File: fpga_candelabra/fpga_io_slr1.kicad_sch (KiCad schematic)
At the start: 1 part, among them U1 XCVU13P-B2104

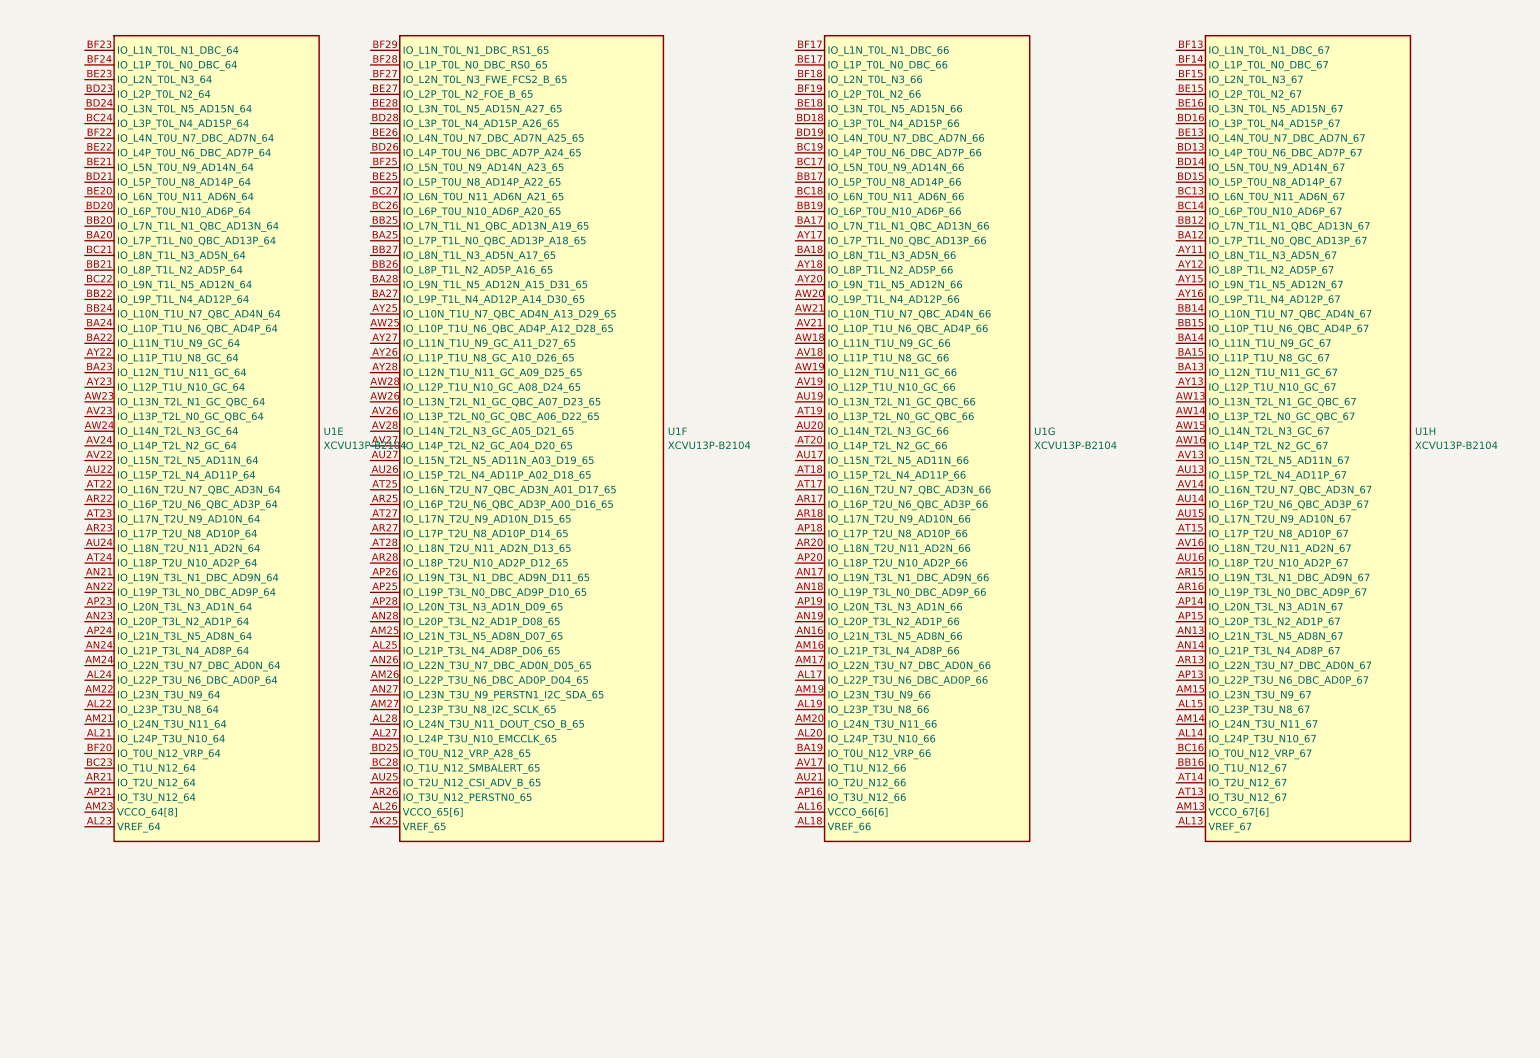
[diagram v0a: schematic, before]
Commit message: candelabra: add i-pex extension ports, remove FMC1
* update bank/mgt allocation
* add basic pcb floorplanning

Signed-off-by: Yichuan Gao <gaoyichuan000@gmail.com>
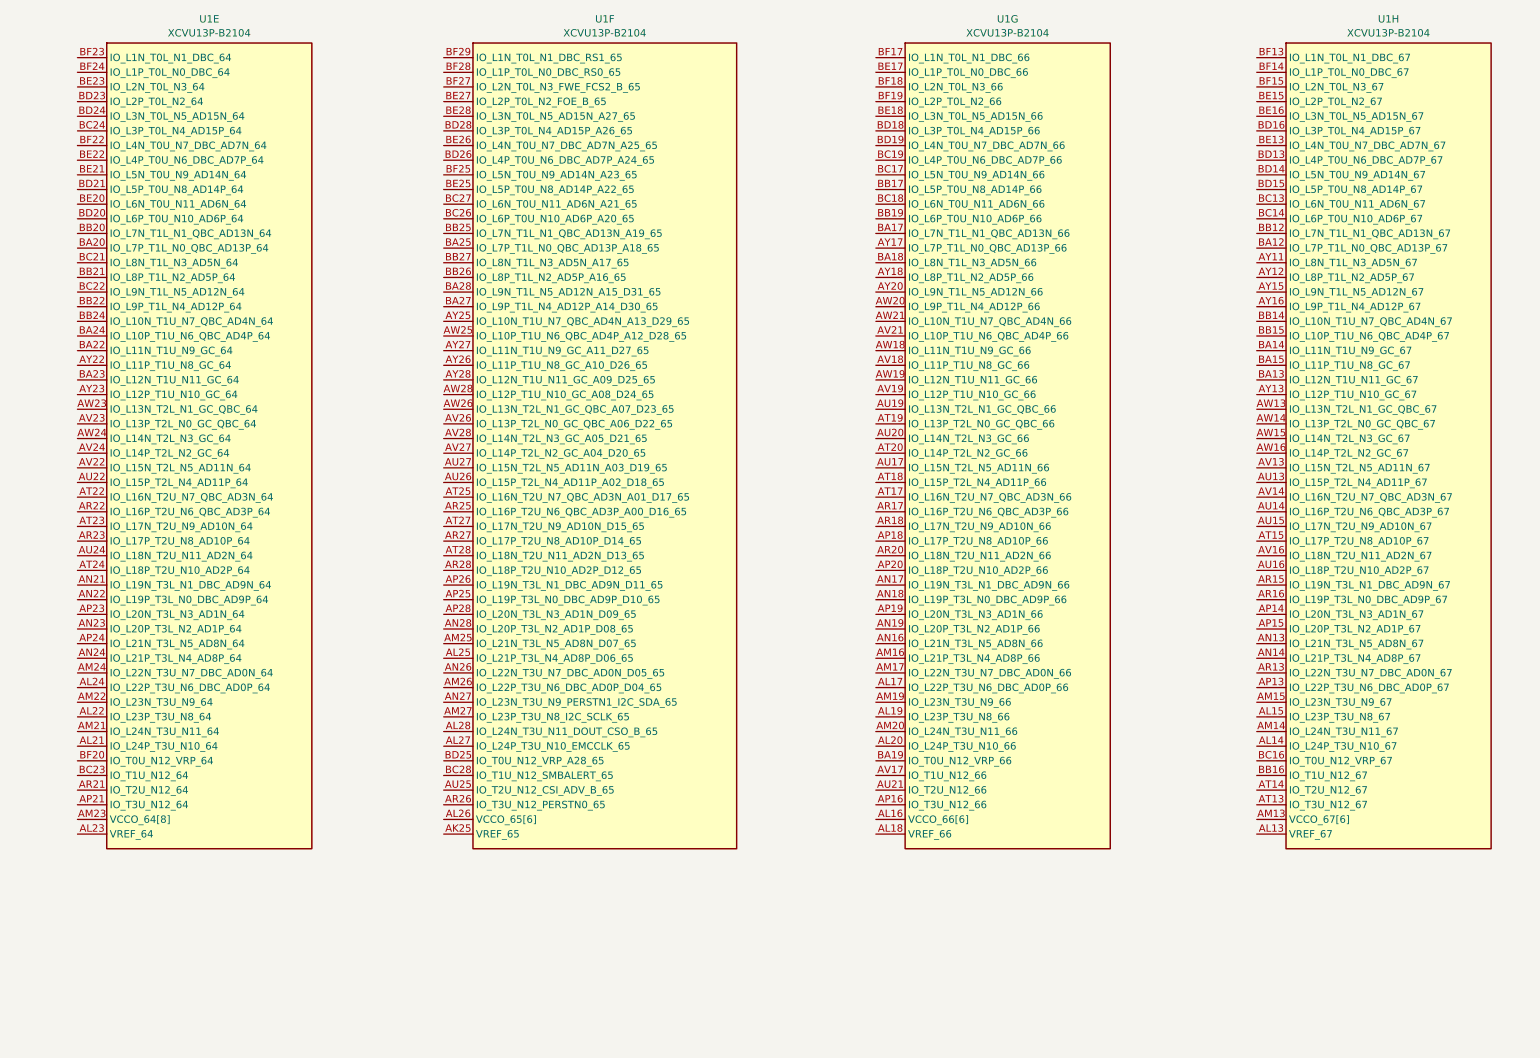
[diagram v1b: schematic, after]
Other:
- moved on the sheet: U1E, U1F, U1G, U1H
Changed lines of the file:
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@@
 	(symbol
 		(lib_id "CHIPSAlliance_FPGA_Xilinx_Virtex_UltraScale_Plus:XCVU13P-B2104")
-		(at 218.44 24.13 0)
+		(at 232.41 25.4 0)
 		(unit 8)
 		(exclude_from_sim no)
@@
 		(fields_autoplaced yes)
 		(property "Reference" "U1"
-			(at 259.842 90.2278 0)
+			(at 255.27 18.7155 0)
 			(effects
 				(font
 					(size 1.27 1.27)
 				)
-				(justify left)
 			)
 		)
 		(property "Value" "XCVU13P-B2104"
-			(at 259.842 92.6521 0)
+			(at 255.27 21.1398 0)
 			(effects
 				(font
 					(size 1.27 1.27)
 				)
-				(justify left)
 			)
 		)
 		(property "Footprint" "CHIPSAlliance_Package_BGA:Xilinx_FHGB2104_VU13P_PkgLength"
-			(at 217.17 22.86 0)
+			(at 231.14 24.13 0)
 			(effects
 				(font
@@
 		)
 		(property "Datasheet" ""
-			(at 217.17 60.96 0)
+			(at 231.14 62.23 0)
 			(effects
 				(font
@@
 		)
 		(property "Description" "Virtex UltraScale+ 13P XCVU13P-B2104"
-			(at 218.44 24.13 0)
+			(at 232.41 25.4 0)
 			(effects
 				(font
@@
 	(symbol
 		(lib_id "CHIPSAlliance_FPGA_Xilinx_Virtex_UltraScale_Plus:XCVU13P-B2104")
-		(at 29.21 24.13 0)
+		(at 27.94 25.4 0)
 		(unit 5)
 		(exclude_from_sim no)
@@
 		(fields_autoplaced yes)
 		(property "Reference" "U1"
-			(at 70.612 90.2278 0)
+			(at 50.8 18.7155 0)
 			(effects
 				(font
 					(size 1.27 1.27)
 				)
-				(justify left)
 			)
 		)
 		(property "Value" "XCVU13P-B2104"
-			(at 70.612 92.6521 0)
+			(at 50.8 21.1398 0)
 			(effects
 				(font
 					(size 1.27 1.27)
 				)
-				(justify left)
 			)
 		)
 		(property "Footprint" "CHIPSAlliance_Package_BGA:Xilinx_FHGB2104_VU13P_PkgLength"
-			(at 27.94 22.86 0)
+			(at 26.67 24.13 0)
 			(effects
 				(font
@@
 		)
 		(property "Datasheet" ""
-			(at 27.94 60.96 0)
+			(at 26.67 62.23 0)
 			(effects
 				(font
@@
 		)
 		(property "Description" "Virtex UltraScale+ 13P XCVU13P-B2104"
-			(at 29.21 24.13 0)
+			(at 27.94 25.4 0)
 			(effects
 				(font
@@
 	(symbol
 		(lib_id "CHIPSAlliance_FPGA_Xilinx_Virtex_UltraScale_Plus:XCVU13P-B2104")
-		(at 152.4 24.13 0)
+		(at 166.37 25.4 0)
 		(unit 7)
 		(exclude_from_sim no)
@@
 		(fields_autoplaced yes)
 		(property "Reference" "U1"
-			(at 193.802 90.2278 0)
+			(at 189.23 18.7155 0)
 			(effects
 				(font
 					(size 1.27 1.27)
 				)
-				(justify left)
 			)
 		)
 		(property "Value" "XCVU13P-B2104"
-			(at 193.802 92.6521 0)
+			(at 189.23 21.1398 0)
 			(effects
 				(font
 					(size 1.27 1.27)
 				)
-				(justify left)
 			)
 		)
 		(property "Footprint" "CHIPSAlliance_Package_BGA:Xilinx_FHGB2104_VU13P_PkgLength"
-			(at 151.13 22.86 0)
+			(at 165.1 24.13 0)
 			(effects
 				(font
@@
 		)
 		(property "Datasheet" ""
-			(at 151.13 60.96 0)
+			(at 165.1 62.23 0)
 			(effects
 				(font
@@
 		)
 		(property "Description" "Virtex UltraScale+ 13P XCVU13P-B2104"
-			(at 152.4 24.13 0)
+			(at 166.37 25.4 0)
 			(effects
 				(font
@@
 	(symbol
 		(lib_id "CHIPSAlliance_FPGA_Xilinx_Virtex_UltraScale_Plus:XCVU13P-B2104")
-		(at 78.74 24.13 0)
+		(at 91.44 25.4 0)
 		(unit 6)
 		(exclude_from_sim no)
@@
 		(fields_autoplaced yes)
 		(property "Reference" "U1"
-			(at 130.302 90.2278 0)
+			(at 119.38 18.7155 0)
 			(effects
 				(font
 					(size 1.27 1.27)
 				)
-				(justify left)
 			)
 		)
 		(property "Value" "XCVU13P-B2104"
-			(at 130.302 92.6521 0)
+			(at 119.38 21.1398 0)
 			(effects
 				(font
 					(size 1.27 1.27)
 				)
-				(justify left)
 			)
 		)
 		(property "Footprint" "CHIPSAlliance_Package_BGA:Xilinx_FHGB2104_VU13P_PkgLength"
-			(at 77.47 22.86 0)
+			(at 90.17 24.13 0)
 			(effects
 				(font
@@
 		)
 		(property "Datasheet" ""
-			(at 77.47 60.96 0)
+			(at 90.17 62.23 0)
 			(effects
 				(font
@@
 		)
 		(property "Description" "Virtex UltraScale+ 13P XCVU13P-B2104"
-			(at 78.74 24.13 0)
+			(at 91.44 25.4 0)
 			(effects
 				(font

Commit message: fpga_candelabra: major revision
* Finish DDR4 & QSFP+ & PCIe layout
* Change FMC to LPC
* Add mikroBUS extension
* 12V input & PDN updates
* FPGA config updates

Signed-off-by: Yichuan Gao <gaoyichuan000@gmail.com>
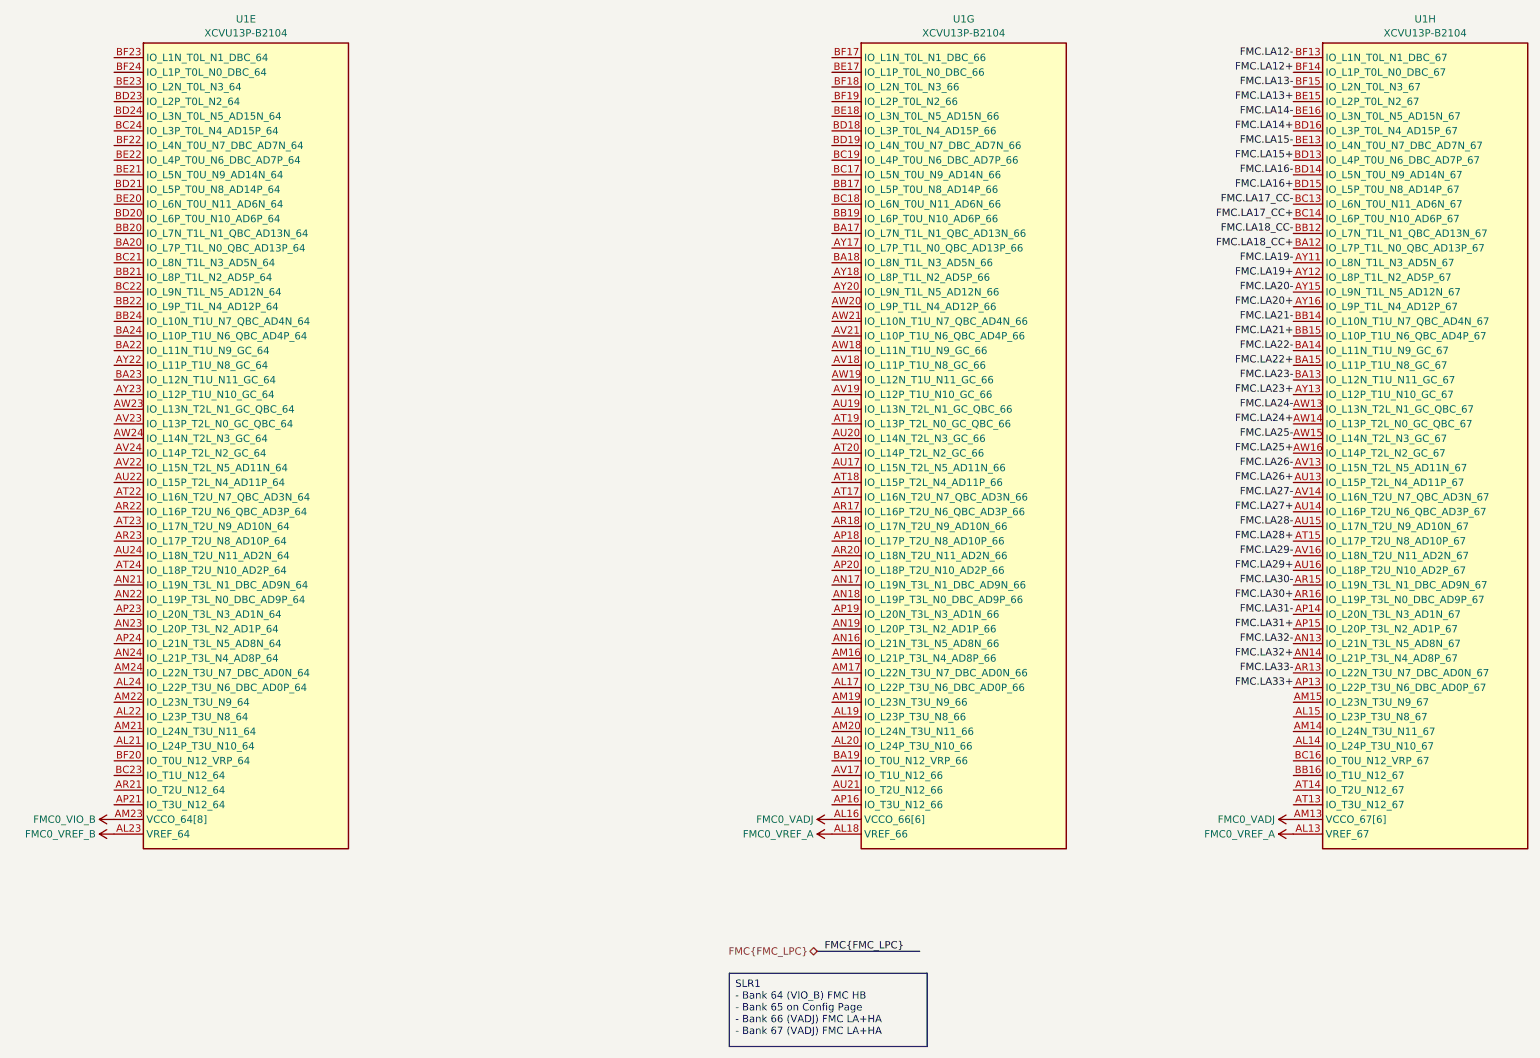
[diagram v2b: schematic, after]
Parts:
- removed unit 6 of U1
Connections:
- net FMC0_VREF_A: now reaches U1.AL13 (VREF_67)
- net FMC0_VREF_A: now also U1.AL18 (VREF_66)
- net FMC0_VADJ: now reaches U1.AM13 (VCCO_67[6]), U1.AR14 (VCCO_67[6]), U1.AV15 (VCCO_67[6]), U1.BA16 (VCCO_67[6]), U1.BB13 (VCCO_67[6]), U1.BE14 (VCCO_67[6])
- net FMC0_VADJ: now also U1.AL16 (VCCO_66[6]), U1.AN20 (VCCO_66[6]), U1.AP17 (VCCO_66[6]), U1.AU18 (VCCO_66[6]), U1.AY19 (VCCO_66[6]), U1.BD17 (VCCO_66[6])
- net FMC.LA32-: now reaches U1.AN13 (IO_L21N_T3L_N5_AD8N_67)
- net FMC.LA32+: now reaches U1.AN14 (IO_L21P_T3L_N4_AD8P_67)
- net FMC.LA33+: now reaches U1.AP13 (IO_L22P_T3U_N6_DBC_AD0P_67)
- net FMC.LA31-: now reaches U1.AP14 (IO_L20N_T3L_N3_AD1N_67)
- net FMC.LA31+: now reaches U1.AP15 (IO_L20P_T3L_N2_AD1P_67)
- net FMC.LA33-: now reaches U1.AR13 (IO_L22N_T3U_N7_DBC_AD0N_67)
- net FMC.LA30-: now reaches U1.AR15 (IO_L19N_T3L_N1_DBC_AD9N_67)
- net FMC.LA30+: now reaches U1.AR16 (IO_L19P_T3L_N0_DBC_AD9P_67)
- net FMC.LA28+: now reaches U1.AT15 (IO_L17P_T2U_N8_AD10P_67)
- net FMC.LA26+: now reaches U1.AU13 (IO_L15P_T2L_N4_AD11P_67)
- net FMC.LA27+: now reaches U1.AU14 (IO_L16P_T2U_N6_QBC_AD3P_67)
- net FMC.LA28-: now reaches U1.AU15 (IO_L17N_T2U_N9_AD10N_67)
- net FMC.LA29+: now reaches U1.AU16 (IO_L18P_T2U_N10_AD2P_67)
- net FMC.LA26-: now reaches U1.AV13 (IO_L15N_T2L_N5_AD11N_67)
- net FMC.LA27-: now reaches U1.AV14 (IO_L16N_T2U_N7_QBC_AD3N_67)
- net FMC.LA29-: now reaches U1.AV16 (IO_L18N_T2U_N11_AD2N_67)
- net FMC.LA24-: now reaches U1.AW13 (IO_L13N_T2L_N1_GC_QBC_67)
- net FMC.LA24+: now reaches U1.AW14 (IO_L13P_T2L_N0_GC_QBC_67)
- net FMC.LA25-: now reaches U1.AW15 (IO_L14N_T2L_N3_GC_67)
- net FMC.LA25+: now reaches U1.AW16 (IO_L14P_T2L_N2_GC_67)
- net FMC.LA19-: now reaches U1.AY11 (IO_L8N_T1L_N3_AD5N_67)
- net FMC.LA19+: now reaches U1.AY12 (IO_L8P_T1L_N2_AD5P_67)
- net FMC.LA23+: now reaches U1.AY13 (IO_L12P_T1U_N10_GC_67)
- net FMC.LA20-: now reaches U1.AY15 (IO_L9N_T1L_N5_AD12N_67)
- net FMC.LA20+: now reaches U1.AY16 (IO_L9P_T1L_N4_AD12P_67)
- net FMC.LA18_CC+: now reaches U1.BA12 (IO_L7P_T1L_N0_QBC_AD13P_67)
- net FMC.LA23-: now reaches U1.BA13 (IO_L12N_T1U_N11_GC_67)
- net FMC.LA22-: now reaches U1.BA14 (IO_L11N_T1U_N9_GC_67)
- net FMC.LA22+: now reaches U1.BA15 (IO_L11P_T1U_N8_GC_67)
- net FMC.LA18_CC-: now reaches U1.BB12 (IO_L7N_T1L_N1_QBC_AD13N_67)
- net FMC.LA21-: now reaches U1.BB14 (IO_L10N_T1U_N7_QBC_AD4N_67)
- net FMC.LA21+: now reaches U1.BB15 (IO_L10P_T1U_N6_QBC_AD4P_67)
- net FMC.LA17_CC-: now reaches U1.BC13 (IO_L6N_T0U_N11_AD6N_67)
- net FMC.LA17_CC+: now reaches U1.BC14 (IO_L6P_T0U_N10_AD6P_67)
- net FMC.LA15+: now reaches U1.BD13 (IO_L4P_T0U_N6_DBC_AD7P_67)
- net FMC.LA16-: now reaches U1.BD14 (IO_L5N_T0U_N9_AD14N_67)
- net FMC.LA16+: now reaches U1.BD15 (IO_L5P_T0U_N8_AD14P_67)
- net FMC.LA14+: now reaches U1.BD16 (IO_L3P_T0L_N4_AD15P_67)
- net FMC.LA15-: now reaches U1.BE13 (IO_L4N_T0U_N7_DBC_AD7N_67)
- net FMC.LA13+: now reaches U1.BE15 (IO_L2P_T0L_N2_67)
- net FMC.LA14-: now reaches U1.BE16 (IO_L3N_T0L_N5_AD15N_67)
- net FMC.LA12-: now reaches U1.BF13 (IO_L1N_T0L_N1_DBC_67)
- net FMC.LA12+: now reaches U1.BF14 (IO_L1P_T0L_N0_DBC_67)
- net FMC.LA13-: now reaches U1.BF15 (IO_L2N_T0L_N3_67)
- net FMC0_VREF_B: now reaches U1.AL23 (VREF_64)
- net FMC0_VIO_B: now reaches U1.AM23 (VCCO_64[8]), U1.AR24 (VCCO_64[8]), U1.AT21 (VCCO_64[8]), U1.AW22 (VCCO_64[8]), U1.BB23 (VCCO_64[8]), U1.BC20 (VCCO_64[8]), U1.BE24 (VCCO_64[8]), U1.BF21 (VCCO_64[8])
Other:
- moved on the sheet: U1E, U1G, U1H
